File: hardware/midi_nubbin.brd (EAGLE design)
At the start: 36.8 x 45.6 mm, 17 parts

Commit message: MN V1 PCB?
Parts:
- removed D3: (no value), adafruit:CHIPLED_0805
- added D1: (no value), adafruit:CHIPLED_0805
- R1: value 4k7 -> (none)
- R2: value (none) -> 4k7
- moved D2 27.9 mm to (30.5, 19.1)
- moved R3 17.2 mm to (29.1, 33.0)
- moved R4 15.6 mm to (22.1, 19.1), turned to 180 degrees
- moved R1 10.9 mm to (22.9, 39.1)
- moved R2 10.9 mm to (31.9, 33.0)
- renumbered U$1 to IC1, U$2 to SW5, U$3 to SW45, U$4 to SW3, U$5 to SW1, U$6 to SW2
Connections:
- net +5V: now also R2.2, R3.2; no longer R1.2, R4.2
- net GND: now also D1.C; no longer D3.C
- net LED1: now also R1.2; no longer R2.2
- net LED2: now also R4.2; no longer R3.2
- net N$1: now also D1.A, R1.1; no longer D2.A, R2.1
- net N$2: now also D2.A, R4.1; no longer D3.A, R3.1
- net N$3: now also R3.1; no longer R4.1
- net RX: now also R2.1; no longer R1.1
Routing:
- net N$2: track 9.27 -> 6.38 mm
- net +5V: track 50.4 -> 49.8 mm
- net GND: vias 5 -> 7
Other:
- outline, holes or cut-outs redrawn
- board text added: "MIDI NUBBIN V1"
- board text added: "hotchk155/2022"

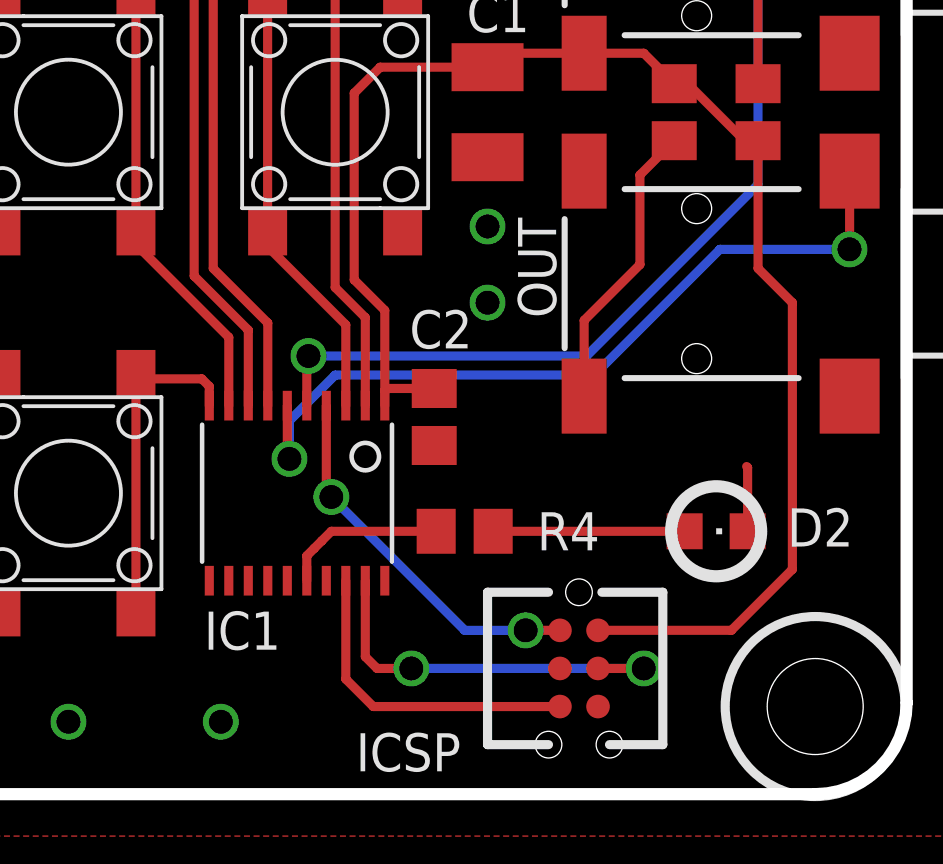
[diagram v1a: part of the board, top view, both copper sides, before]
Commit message: Change SSOP footprint
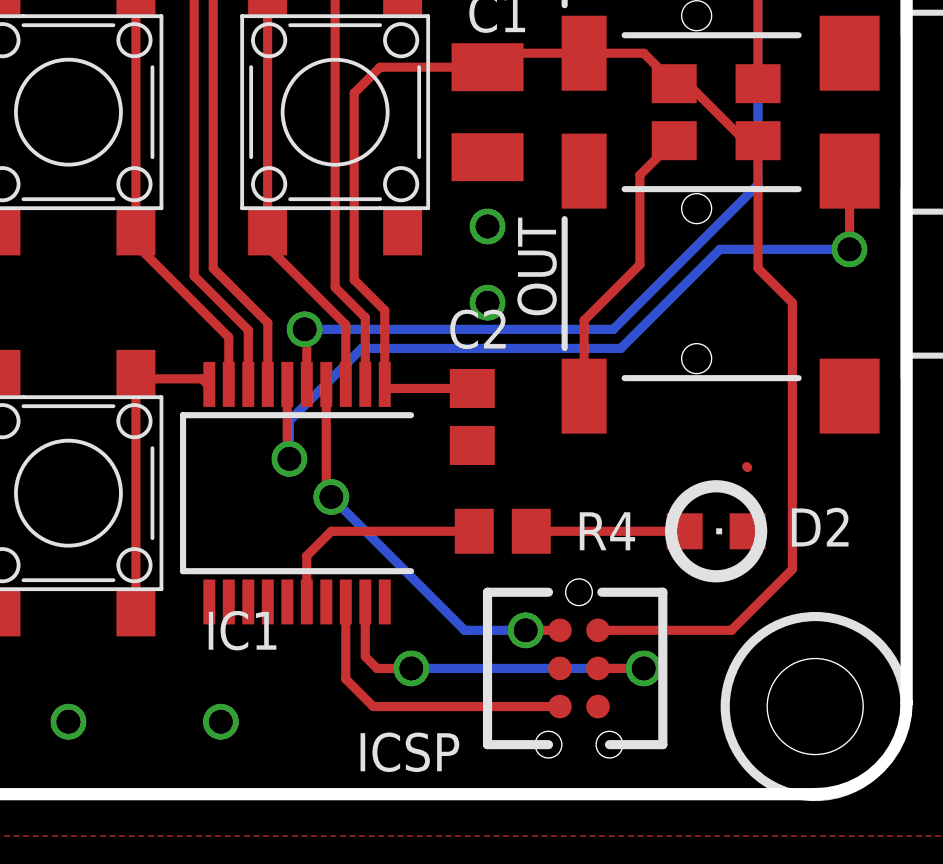
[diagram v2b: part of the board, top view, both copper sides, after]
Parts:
- IC1: value PIC16F15345 -> PIC16F15345SSOP20; device jason_eagle6:TSSOP20 -> jason_eagle6:SSOP20
- moved C2 1.27 mm to (22.4, 22.9)
- moved R4 1.27 mm to (23.4, 19.1)
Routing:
- net GND: track 3.66 -> 1.54 mm
- net LED2: track 5.48 -> 7.46 mm
- net N$2: track 6.38 -> 5.11 mm
- net +5V: track 49.8 -> 50.6 mm
- net VPP: track 12.6 -> 13.3 mm
- net TX: track 26.7 -> 27.4 mm
- net PGD: track 13.5 -> 12.8 mm
- net PGC: track 10.8 -> 10.1 mm
- net LED1: track 20.9 -> 20.2 mm
- net KEY4: track 15.4 -> 14.7 mm
- net KEY3: track 28.4 -> 27.7 mm
- net KEY2: track 28.4 -> 27.7 mm
- net KEY1: track 14.9 -> 14.2 mm
- net KEY5: track 11.3 -> 10.7 mm

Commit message: BOARD V2
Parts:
- added R5: 220, rcl:R0805
- added R6: (no value), rcl:R0805
- R2: value 4k7 -> 220
- R3: value (none) -> 4k7
- moved R2 14.9 mm to (24.1, 45.7), turned to 0 degrees
- moved R1 9.23 mm to (24.1, 48.3), turned to 180 degrees
- moved R3 8.80 mm to (23.0, 39.4), turned to 0 degrees
- moved R4 7.26 mm to (22.9, 26.3)
- moved C2 1.02 mm to (22.9, 23.7), turned to 0 degrees
- moved C1 0.25 mm to (22.9, 32.8)
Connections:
- new net N$4: OUT.2, R5.1
- new net N$5: IN.2, R2.2
- net +5V: now also R4.2; no longer R2.2
- net LED2: now also R6.2; no longer R4.2
- net N$2: now also R6.1; no longer R4.1
- net N$3: now also R4.1; no longer R3.1
- net RX: now also R3.1; no longer IN.2
- net TX: now also R5.2; no longer OUT.2
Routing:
- net N$4: track 0.00 -> 21.2 mm
- net TX: track 27.4 -> 9.53 mm, vias 2 -> 0
- net N$5: track 0.00 -> 12.5 mm
- net N$1: track 12.0 -> 4.88 mm
- net LED1: track 20.2 -> 27.1 mm, vias 0 -> 2
- net RX: track 36.9 -> 30.9 mm, vias 2 -> 0
- net N$3: track 9.76 -> 5.66 mm
- net +5V: track 50.6 -> 49.8 mm, vias 0 -> 2
- net N$2: track 5.11 -> 5.73 mm
- net LED2: track 7.46 -> 6.85 mm
- net KEY2: track 27.7 -> 28.3 mm
- net GND: vias 7 -> 8
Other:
- board text added: "MIDI NUBBIN V2"
- board text removed: "MIDI NUBBIN V1"

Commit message: v3
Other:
- board size 36.8 x 45.6 mm -> 40 x 48.1 mm
- board text added: "MIDI NUBBIN V3"
- board text removed: "MIDI NUBBIN V2"
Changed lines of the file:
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@@
 <setting verticaltext="up"/>
 </settings>
-<grid distance="0.05" unitdist="inch" unit="inch" style="lines" multiple="1" display="no" altdistance="0.005" altunitdist="inch" altunit="inch"/>
+<grid distance="0.05" unitdist="inch" unit="mm" style="lines" multiple="1" display="no" altdistance="0.005" altunitdist="inch" altunit="inch"/>
 <layers>
 <layer number="1" name="Top" color="4" fill="1" visible="yes" active="yes"/>
@@
 <hole x="33.782" y="52.832" drill="3.2"/>
 <hole x="33.782" y="13.208" drill="3.2"/>
-<wire x1="3.048" y1="55.88" x2="3.175" y2="55.88" width="0.4064" layer="20"/>
-<wire x1="3.175" y1="55.88" x2="32.512" y2="55.88" width="0.4064" layer="20"/>
-<wire x1="32.512" y1="55.88" x2="36.83" y2="52.705" width="0.4064" layer="20" curve="-92.338267"/>
-<wire x1="36.83" y1="52.705" x2="36.83" y2="13.335" width="0.4064" layer="20"/>
-<wire x1="36.83" y1="13.335" x2="33.782" y2="10.287" width="0.4064" layer="20" curve="-90"/>
-<wire x1="33.782" y1="10.287" x2="2.921" y2="10.287" width="0.4064" layer="20"/>
-<wire x1="2.921" y1="10.287" x2="0" y2="13.208" width="0.4064" layer="20" curve="-90"/>
-<wire x1="0" y1="13.208" x2="0" y2="52.705" width="0.4064" layer="20"/>
-<wire x1="0" y1="52.705" x2="3.175" y2="55.88" width="0.4064" layer="20" curve="-90"/>
+<wire x1="3.048" y1="57.1235" x2="33.782" y2="57.1235" width="0.4064" layer="20"/>
+<wire x1="33.782" y1="57.1235" x2="38.43" y2="52.832" width="0.4064" layer="20" curve="-92.338267"/>
+<wire x1="38.43" y1="52.832" x2="38.43" y2="13.208" width="0.4064" layer="20"/>
+<wire x1="38.43" y1="13.208" x2="33.782" y2="9.0435" width="0.4064" layer="20" curve="-90"/>
+<wire x1="33.782" y1="9.0435" x2="3.048" y2="9.0435" width="0.4064" layer="20"/>
+<wire x1="3.048" y1="9.0435" x2="-1.6" y2="13.208" width="0.4064" layer="20" curve="-90"/>
+<wire x1="-1.6" y1="13.208" x2="-1.6" y2="52.832" width="0.4064" layer="20"/>
+<wire x1="-1.6" y1="52.832" x2="3.048" y2="57.1235" width="0.4064" layer="20" curve="-90"/>
 <circle x="3.048" y="52.832" radius="3" width="0.3048" layer="21"/>
 <circle x="33.782" y="52.832" radius="3" width="0.3048" layer="21"/>
 <circle x="33.782" y="13.208" radius="3" width="0.3048" layer="21"/>
 <circle x="3.048" y="13.208" radius="3" width="0.3048" layer="21"/>
-<text x="1.143" y="47.879" size="2.54" layer="47" font="vector" ratio="20" rot="SR270">MIDI NUBBIN V2</text>
+<text x="1.143" y="47.879" size="2.54" layer="47" font="vector" ratio="20" rot="SR270">MIDI NUBBIN V3</text>
 <text x="7.366" y="53.34" size="1.778" layer="47" font="vector" ratio="20" rot="SR0">hotchk155/2022</text>
 <wire x1="24.892" y1="17.018" x2="22.86" y2="17.018" width="0.3048" layer="21"/>

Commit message: add logo
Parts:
- moved D1 9.24 mm to (32.1, 37.9)
- moved D2 9.24 mm to (32.1, 9.95)
- moved ICSP 9.24 mm to (27.5, 7.92)
- moved OUT 9.24 mm to (38.4, 18.2)
- moved R1 9.24 mm to (25.7, 39.2)
- moved R2 9.24 mm to (25.7, 36.6)
- moved R4 9.24 mm to (24.5, 17.2)
- moved SW1 9.24 mm to (19.4, 36.6)
- moved SW2 9.24 mm to (19.4, 23.9)
- moved SW3 9.24 mm to (10.5, 36.6)
- moved SW45 9.24 mm to (10.5, 23.9)
- moved C2 9.24 mm to (24.5, 14.6)
- moved IC1 9.24 mm to (18.1, 11.2)
- moved R5 9.24 mm to (24.5, 12.1)
- moved R6 9.24 mm to (24.5, 9.70)
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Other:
- board size 40 x 48.1 mm -> 40 x 48 mm
